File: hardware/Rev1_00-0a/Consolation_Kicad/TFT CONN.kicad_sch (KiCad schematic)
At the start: 42 parts, among them J3 62684-402100ALF, J9 5051101092, U26 TPS61169DCKR

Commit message: Add part number of codec to block diagram Add codec and hdmi schematic sheets
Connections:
- net 3V3_CB renamed 3V3
- net 5V0_CB renamed 5V0

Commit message: Update schematics, block diagram and pin mux (good progress G)
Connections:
- net USB_HOST.USB_N renamed USB2_CTP.USB_N
- net USB_HOST.USB_P renamed USB2_CTP.USB_P
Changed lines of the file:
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@@
 	(text "Resistors are 1% 1/16W 0402 unless otherwise noted\nCapacitors are 10% 50V X7R 0402 unless otherwise noted"
 		(exclude_from_sim no)
-		(at 12.7 170.307 0)
+		(at 12.7 170.942 0)
 		(effects
 			(font
@@
 		)
 	)
-	(label "USB_HOST.USB_N"
+	(label "USB2_CTP.USB_N"
 		(at 146.685 19.685 0)
 		(effects
@@
 		)
 	)
-	(label "USB_HOST.USB_P"
+	(label "USB2_CTP.USB_P"
 		(at 146.685 22.225 0)
 		(effects
@@
 		)
 	)
-	(hierarchical_label "USB_HOST{USB2}"
+	(hierarchical_label "USB2_CTP{USB2}"
 		(shape bidirectional)
 		(at 114.3 14.605 180)

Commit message: Update PinMux & Schematics
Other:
- moved on the sheet: C162, C163, C164, C165, C166, D30, L5, R208, R210, R305, R306, TP28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

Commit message: Commit ConJoy design + output files (ready for manufacturing or REV 1.00-0A)
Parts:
- removed MTG5, MTG6, MTG7, MTG8: M0504-25-AL-7, footprint:M0504-25-AL-7, symbol KicadCompDb:Miscellaneous/MISC_00004

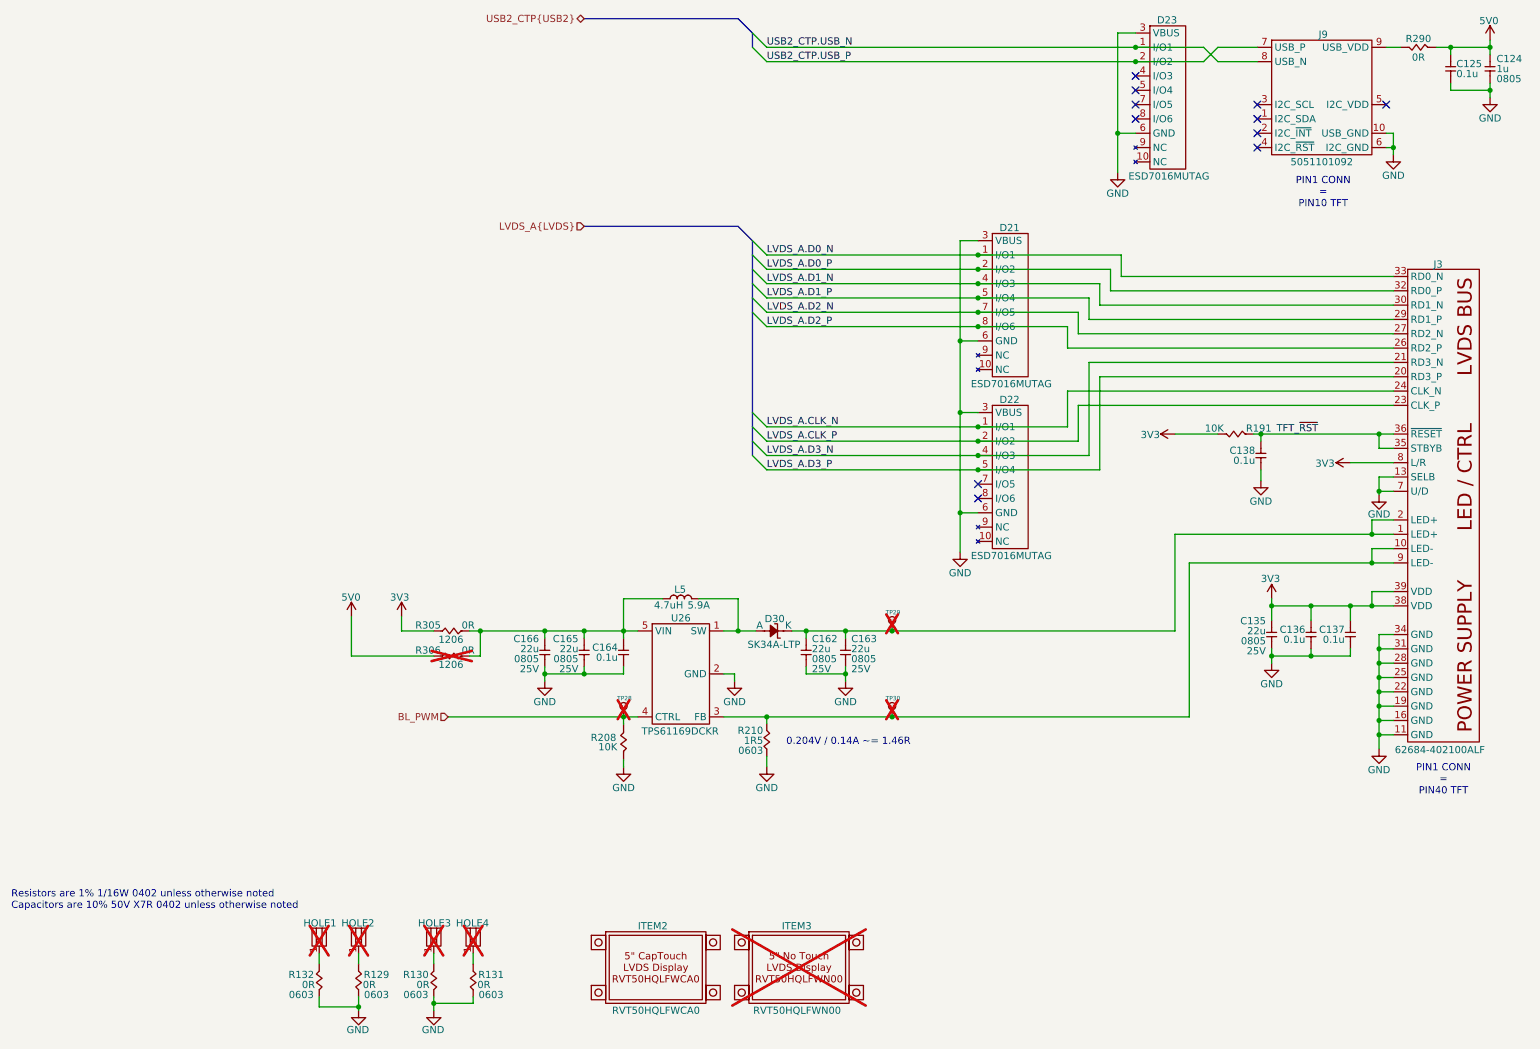
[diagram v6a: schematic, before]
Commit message: Major update to consolation schematics to include - Power supply - RESET SUPERVISOR - Review of GPIO and pinmux
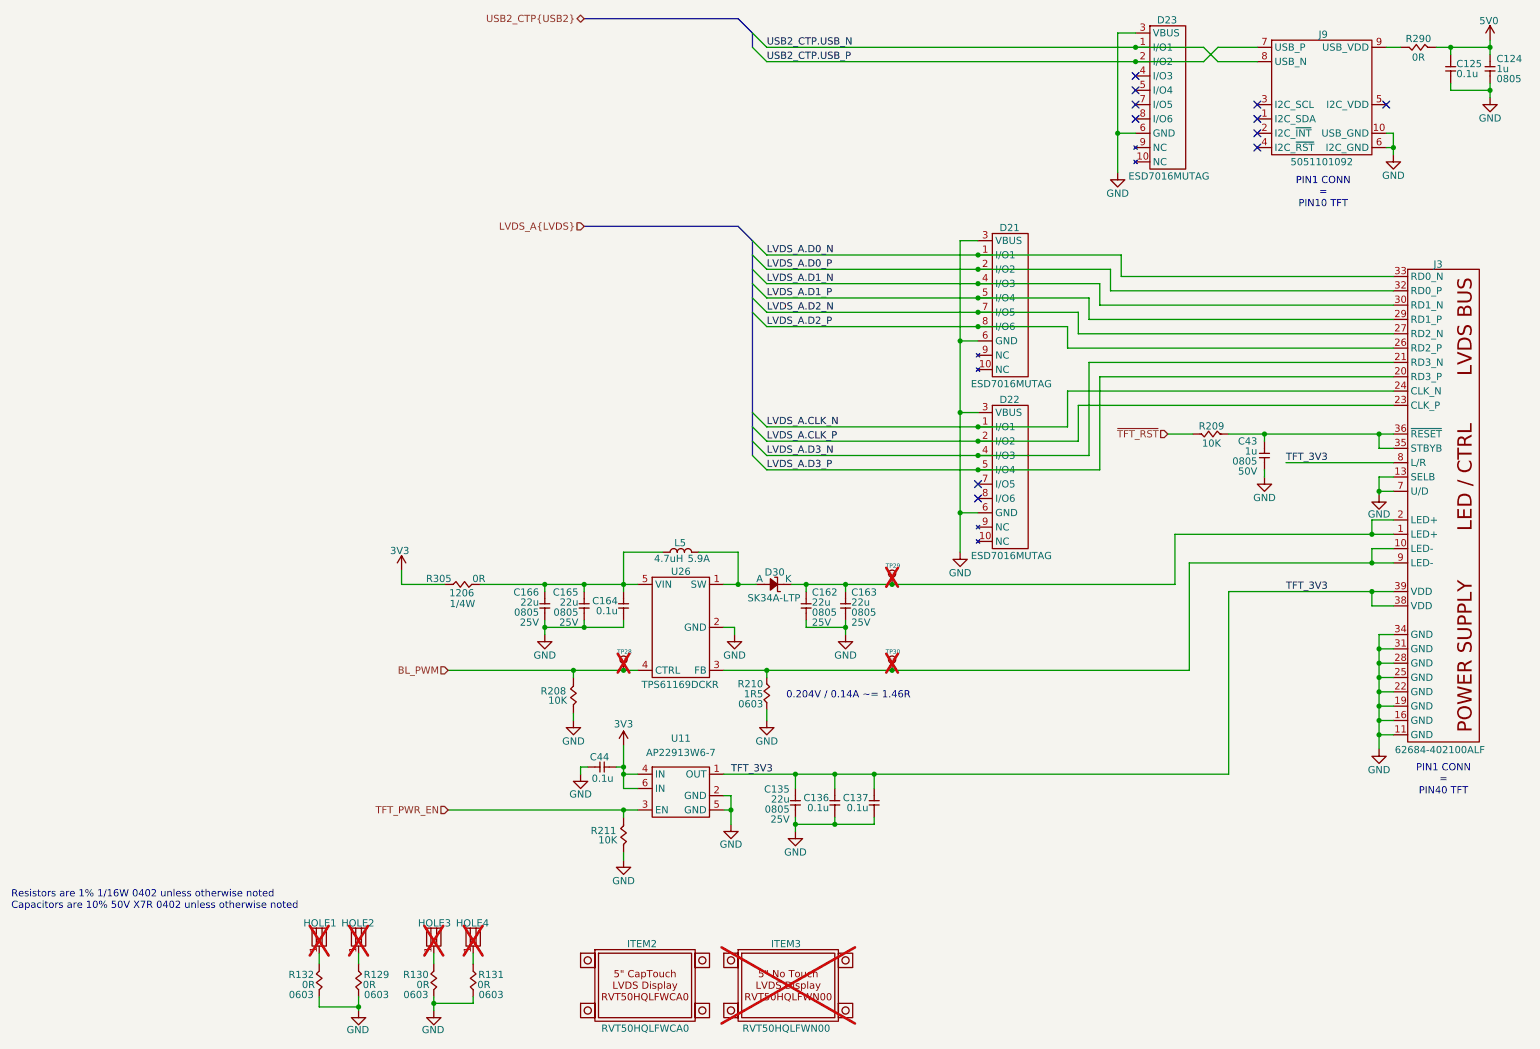
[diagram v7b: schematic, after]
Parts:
- removed C138: 0.1u, footprint:CAP_NONPOL_0402, symbol KicadCompDb:Capacitors/CAP_CER_SMT_00001
- removed R191: 10K, footprint:RES_0402, symbol KicadCompDb:Resistors/RES_SMT_00013
- removed R306: 0R, footprint:RES_1206, symbol KicadCompDb:Resistors/RES_SMT_00022
- added C43: 1u, footprint:CAP_NONPOL_0805, symbol KicadCompDb:Capacitors/CAP_CER_SMT_00002
- added C44: 0.1u, footprint:CAP_NONPOL_0402, symbol KicadCompDb:Capacitors/CAP_CER_SMT_00001
- added R209, R211: 10K, footprint:RES_0402, symbol KicadCompDb:Resistors/RES_SMT_00013
- added U11: AP22913W6-7, footprint:SOT-23-6, symbol KicadCompDb:Load Switch/LOAD_SW_00001
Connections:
- net 3V3: now also C44.2, U11.4 (IN), U11.6 (IN); no longer C135.2, C136.2, C137.2, J3.38 (VDD), J3.39 (VDD), J3.8 (L/R)
- net GND: now also C43.1, C44.1, R211.1, U11.2 (GND), U11.5 (GND)
- net TFT_~{RST}: no longer names the net of J3.35 (STBYB), J3.36 (~{RESET})
- net TFT_~{RST}: now also C43.2, R209.1
- new net TFT_3V3: C135.2, C136.2, C137.2, J3.38 (VDD), J3.39 (VDD), J3.8 (L/R), U11.1 (OUT)
- new net TFT_PWR_EN: R211.2, U11.3 (EN)
- new net ~{TFT_RST}: R209.2
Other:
- moved on the sheet: C162, C163, C164, C165, C166, D30, ITEM2, ITEM3, L5, R208, R210, R305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

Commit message: Removed unnecessary functions (USB2 mux, CapTouch) Adjusted 220uF alum capacitor for codec (slimmer version)
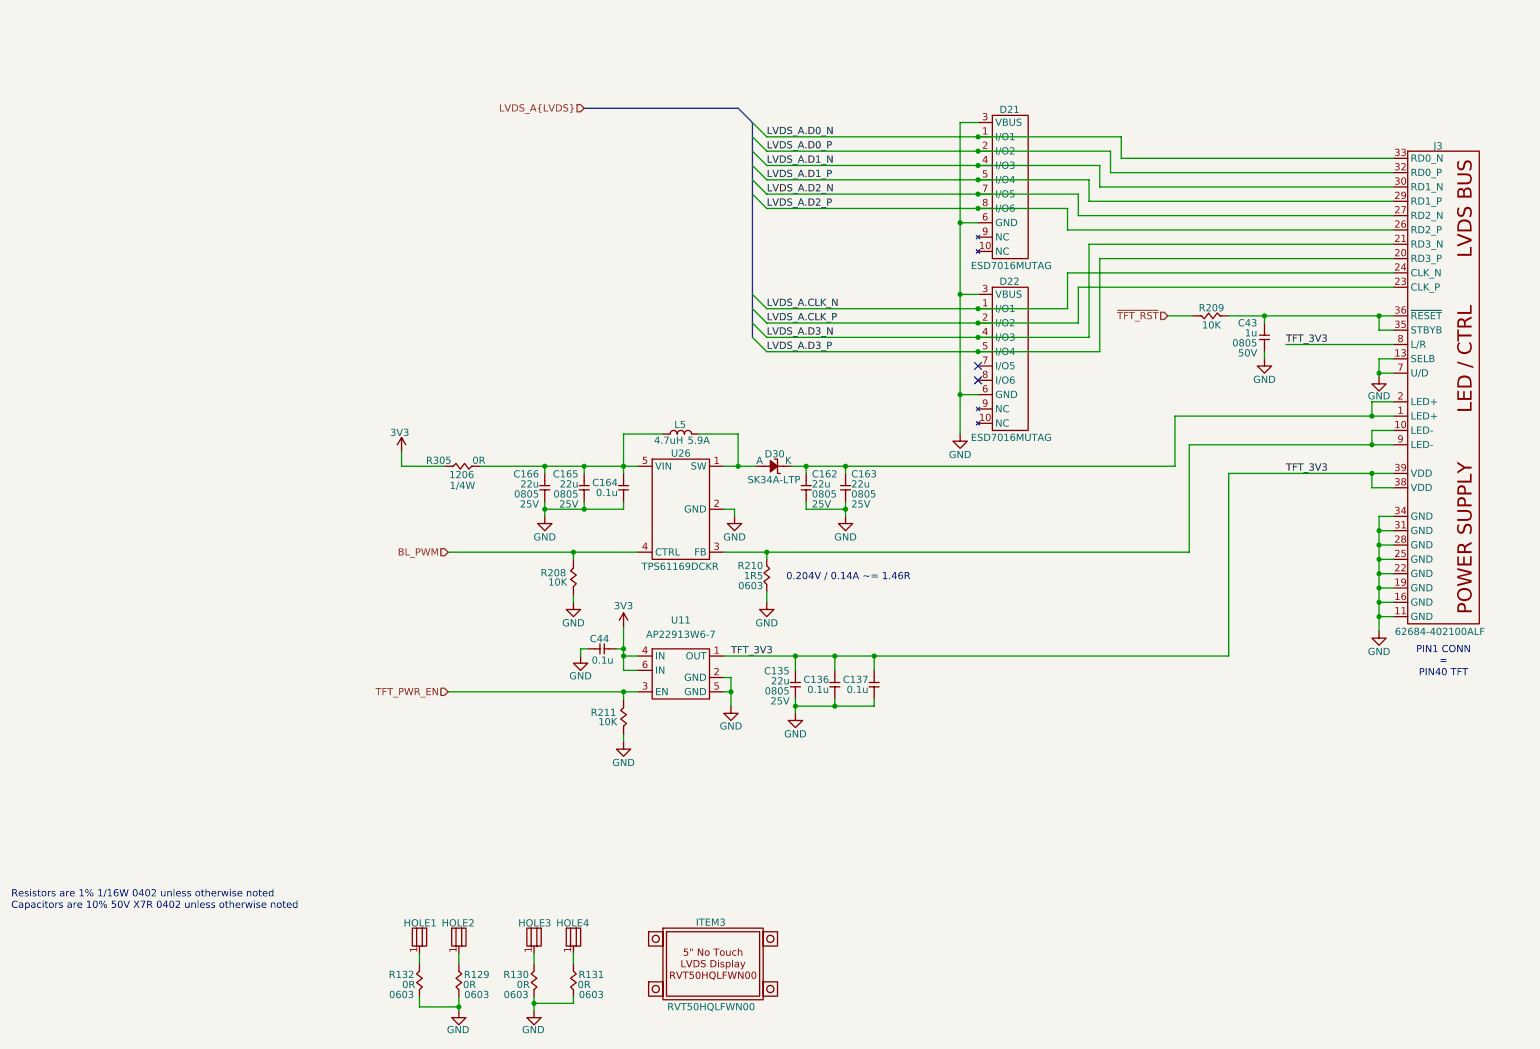
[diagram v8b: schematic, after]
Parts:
- removed C124: 1u, footprint:CAP_NONPOL_0805, symbol KicadCompDb:Capacitors/CAP_CER_SMT_00002
- removed C125: 0.1u, footprint:CAP_NONPOL_0402, symbol KicadCompDb:Capacitors/CAP_CER_SMT_00001
- removed D23: ESD7016MUTAG, footprint:UDFN8, symbol KicadCompDb:ESD Diodes/ESD_DIODE_00001
- removed ITEM2: RVT50HQLFWCA0, footprint:RVT50HQLFWCA0, symbol KicadCompDb:Miscellaneous/MISC_00011
- removed J9: 5051101092, footprint:5051101092, symbol KicadCompDb:Connector/CONN_00017
- removed R290: 0R, footprint:RES_0402, symbol KicadCompDb:Resistors/RES_SMT_00001
- removed TP28, TP29, TP30: 28 mils, footprint:SMT_TP_28_MILS, symbol KicadCompDb:Test Point/TP_00001
- HOLE1, HOLE2, HOLE3, HOLE4: footprint MTG_hole_cir_5mm_pad_3mm_drill -> footprint:MTG_hole_cir_5mm_pad_3mm_drill; now fitted
- ITEM3: now fitted
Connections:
- no-connect marks 11 -> 2
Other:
- note removed: "PIN1 CONN = PIN10 TFT"
- moved on the sheet: C135, C136, C137, C162, C163, C164, C165, C166, C43, C44, D21, D22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
